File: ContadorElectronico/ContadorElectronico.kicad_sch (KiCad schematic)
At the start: 27 parts, among them J1 Screw_Terminal_01x02, J2 Screw_Terminal_01x02, SW1 MODE, SW2 INC, SW3 DEC, U4 LM358, U5 4N35, U6 4N35

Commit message: First PCB design
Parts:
- removed F?: Fuse, symbol Device:Fuse
- J1: value Screw_Terminal_01x02 -> POWER
- J2: value Screw_Terminal_01x02 -> INPUT
- gave numbers to parts that had none: 1
- renumbered D2 to #D1, D1 to D2, U1 to U2
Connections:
- net +5V: now also J1.1 (Pin_1)
- net GND: now also #U1.2 (IN-), J1.2 (Pin_2)
- net +24V: now reaches #D1.2 (A)
- net +24V: no longer J1.1 (Pin_1)
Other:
- note added: "POWER CONDITIONING"
- moved on the sheet: A1, D2, J1, J2, R1, R10, R11, R12, R2, R3, R4, R5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

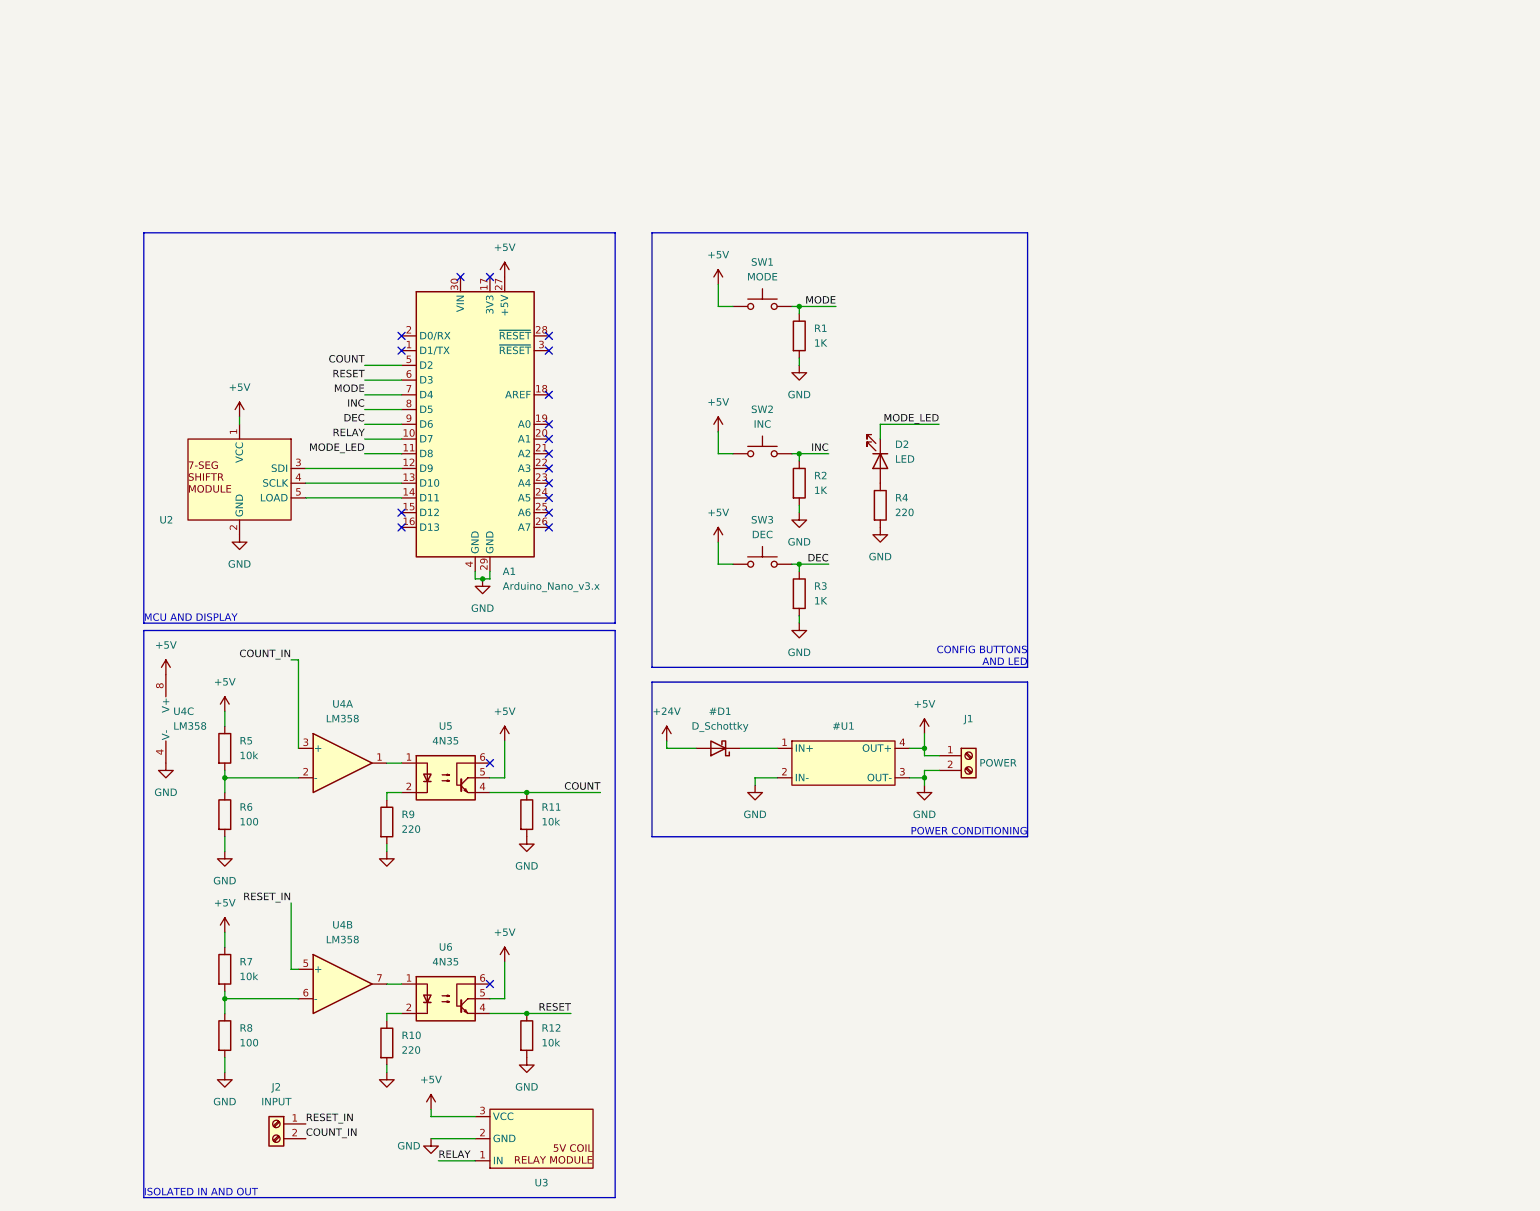
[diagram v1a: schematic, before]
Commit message: PCB done, 5V direct to Arduino
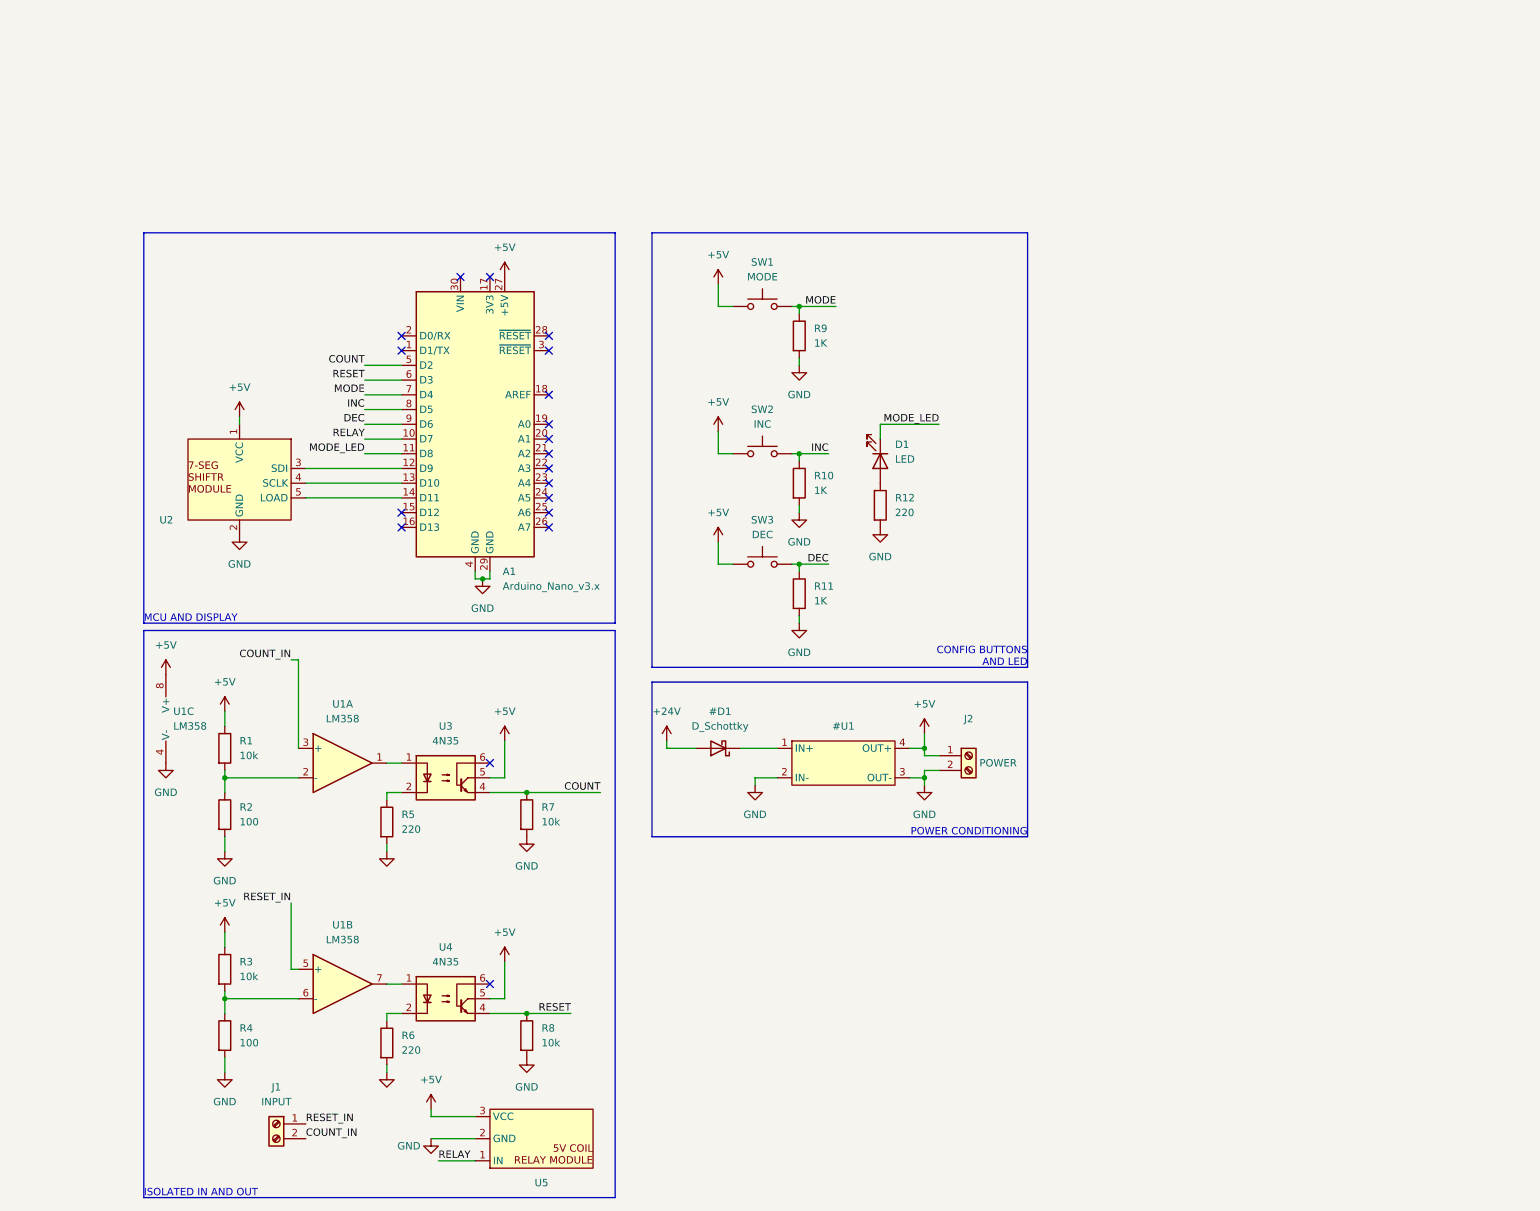
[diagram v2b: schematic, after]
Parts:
- renumbered D2 to D1, J2 to J1, J1 to J2, R5 to R1, R2 to R10, R3 to R11, R4 to R12, R6 to R2, R7 to R3, R8 to R4, R9 to R5, R10 to R6, R11 to R7, R12 to R8, R1 to R9, U4 to U1, U5 to U3, U6 to U4, U3 to U5

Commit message: Diseño inicial
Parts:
- removed #D1: D_Schottky, Diode_THT:D_DO-15_P12.70mm_Horizontal, symbol Device:D_Schottky
- removed J1: INPUT, TerminalBlock:TerminalBlock_bornier-2_P5.08mm, symbol Connector:Screw_Terminal_01x02
- removed J2: POWER, TerminalBlock:TerminalBlock_bornier-2_P5.08mm, symbol Connector:Screw_Terminal_01x02
- added D1: 1N4002, Diode_THT:D_DO-41_SOD81_P10.16mm_Horizontal, symbol Diode:1N4002
- added J1: Screw_Terminal_01x03, TerminalBlock:TerminalBlock_bornier-3_P5.08mm, symbol Connector:Screw_Terminal_01x03
- added J2, J3, J4, J5, J6, J7, J8: Conn_01x01_Pin, Connector:Banana_Jack_1Pin, symbol Connector:Conn_01x01_Pin
- R1, R10, R11, R12, R2, R3, R4, R5, R6, R7, R8, R9: footprint Resistor_THT:R_Axial_DIN0207_L6.3mm_D2.5mm_P10.16mm_Horizontal -> Resistor_SMD:R_0603_1608Metric_Pad0.98x0.95mm_HandSolder
- SW1_MODE1: renamed from SW1; footprint Custom:SW Header -> Button_Switch_THT:SW_PUSH_6mm
- SW2_INC1: renamed from SW2; footprint Custom:SW Header -> Button_Switch_THT:SW_PUSH_6mm
- SW3_DEC1: renamed from SW3; footprint Custom:SW Header -> Button_Switch_THT:SW_PUSH_6mm
- U2: footprint Connector_PinSocket_2.54mm:PinSocket_1x05_P2.54mm_Vertical -> Custom:2Digit7SEG
- U6: renamed from #U1; footprint (none) -> Custom:LM2596 MODULE
- renumbered D1 to D2
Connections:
- net +24V: now also D1.2 (A), J7.1 (Pin_1)
- net +5V: no longer U6.4 (OUT+)
- net COUNT_IN: now also J6.1 (Pin_1)
- net GND: now also J8.1 (Pin_1)
- net RESET_IN: now also J2.1 (Pin_1)
- net at U6.1 (IN+): now also D1.1 (K)
- net +9V: now reaches A1.30 (VIN)
- net +9V: now also U6.4 (OUT+)
- new net COM: J1.2 (Pin_2), J4.1 (Pin_1)
- new net NC: J1.1 (Pin_1), J3.1 (Pin_1)
- new net NO: J1.3 (Pin_3), J5.1 (Pin_1)
- no-connect marks 19 -> 18

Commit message: Working version #1
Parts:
- removed J6: Conn_01x01_Pin, Connector:Banana_Jack_1Pin, symbol Connector:Conn_01x01_Pin
- removed R1, R3: 10k, Resistor_SMD:R_0603_1608Metric_Pad0.98x0.95mm_HandSolder, symbol Device:R
- removed R2, R4: 100, Resistor_SMD:R_0603_1608Metric_Pad0.98x0.95mm_HandSolder, symbol Device:R
- removed U1: LM358, Package_DIP:DIP-8_W7.62mm_Socket, symbol Amplifier_Operational:LM358
- added J1: Conn_01x01_Pin, Connector:Banana_Jack_1Pin, symbol Connector:Conn_01x01_Pin
- R1: renamed from R5; value 220 -> 10k; footprint Resistor_SMD:R_0603_1608Metric_Pad0.98x0.95mm_HandSolder -> Resistor_SMD:R_1206_3216Metric_Pad1.30x1.75mm_HandSolder
- R2: renamed from R6; value 220 -> 10k; footprint Resistor_SMD:R_0603_1608Metric_Pad0.98x0.95mm_HandSolder -> Resistor_SMD:R_1206_3216Metric_Pad1.30x1.75mm_HandSolder
- R3: renamed from R7; footprint Resistor_SMD:R_0603_1608Metric_Pad0.98x0.95mm_HandSolder -> Resistor_SMD:R_1206_3216Metric_Pad1.30x1.75mm_HandSolder
- R4: renamed from R8; footprint Resistor_SMD:R_0603_1608Metric_Pad0.98x0.95mm_HandSolder -> Resistor_SMD:R_1206_3216Metric_Pad1.30x1.75mm_HandSolder
- R5: renamed from R9; footprint Resistor_SMD:R_0603_1608Metric_Pad0.98x0.95mm_HandSolder -> Resistor_SMD:R_1206_3216Metric_Pad1.30x1.75mm_HandSolder
- R6: renamed from R10; footprint Resistor_SMD:R_0603_1608Metric_Pad0.98x0.95mm_HandSolder -> Resistor_SMD:R_1206_3216Metric_Pad1.30x1.75mm_HandSolder
- R7: renamed from R11; footprint Resistor_SMD:R_0603_1608Metric_Pad0.98x0.95mm_HandSolder -> Resistor_SMD:R_1206_3216Metric_Pad1.30x1.75mm_HandSolder
- R8: renamed from R12; footprint Resistor_SMD:R_0603_1608Metric_Pad0.98x0.95mm_HandSolder -> Resistor_SMD:R_1206_3216Metric_Pad1.30x1.75mm_HandSolder
- renumbered J1 to J3, J3 to J4, J4 to J5, J5 to J6, U2 to U1, U3 to U2, U4 to U3, U5 to U4, U6 to U5
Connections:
- net +5V: now also U5.4 (OUT+)
- net COUNT: now also A1.6 (D3); no longer A1.5 (D2)
- net COUNT_IN: now also J2.1 (Pin_1), U2.1
- net DEC: now also A1.8 (D5); no longer A1.9 (D6)
- net INC: now also A1.10 (D7); no longer A1.8 (D5)
- net MODE: now also A1.11 (D8); no longer A1.7 (D4)
- net MODE_LED: now also A1.9 (D6); no longer A1.11 (D8)
- net RELAY: now also A1.7 (D4); no longer A1.10 (D7)
- net RESET: now also A1.5 (D2); no longer A1.6 (D3)
- net RESET_IN: now also U3.1, J1.1 (Pin_1); no longer J2.1 (Pin_1)
- net at A1.12 (D9): now also U1.5 (LOAD); no longer U1.3 (SDI)
- net at A1.14 (D11): now also U1.3 (SDI); no longer U1.5 (LOAD)
- net +24V: no longer names the net of D1.2 (A), J7.1 (Pin_1)
- net +9V: no longer names the net of A1.30 (VIN)
- net +9V: no longer U5.4 (OUT+)
- no-connect marks 18 -> 19
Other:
- moved on the sheet: J3, J4, J5, J6, R1, R2, R3, R4, U2, U3, U4

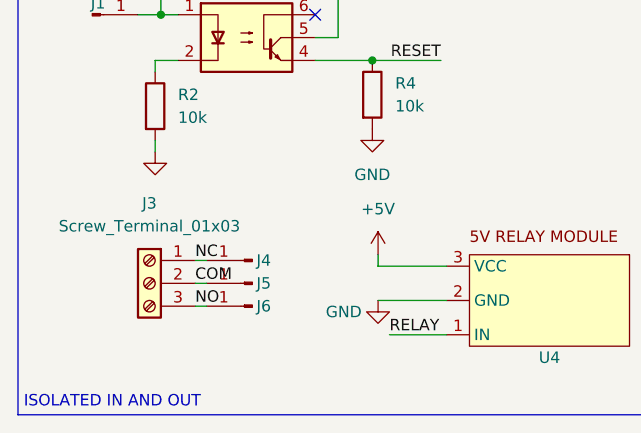
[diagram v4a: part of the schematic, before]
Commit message: ajustes a la PCB
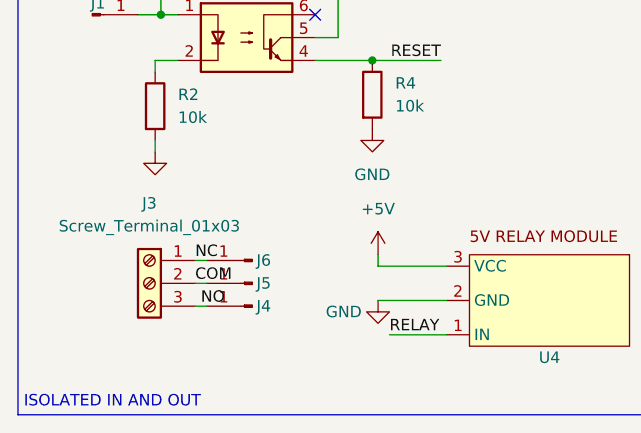
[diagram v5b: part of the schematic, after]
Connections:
- net NC: now also J6.1 (Pin_1); no longer J4.1 (Pin_1)
- net NO: now also J4.1 (Pin_1); no longer J6.1 (Pin_1)
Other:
- moved on the sheet: J4, J6
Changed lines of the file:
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@@
+    (stroke (width 0) (type default))
+  )
+  (wire (pts (xy 53.975 195.58) (xy 55.245 195.58))
     (stroke (width 0) (type default))
   )
@@
     (stroke (width 0) (type default))
   )
-  (wire (pts (xy 53.975 195.58) (xy 55.245 195.58))
-    (stroke (width 0) (type default))
-  )
   (wire (pts (xy 67.31 168.275) (xy 73.66 168.275))
     (stroke (width 0) (type default))
@@
     (stroke (width 0) (type default))
   )
+  (wire (pts (xy 69.85 99.06) (xy 69.85 93.98))
+    (stroke (width 0) (type default))
+  )
+  (wire (pts (xy 161.29 86.36) (xy 161.29 88.9))
+    (stroke (width 0) (type default))
+  )
+  (wire (pts (xy 147.32 111.76) (xy 147.32 110.49))
+    (stroke (width 0) (type default))
+  )
+  (wire (pts (xy 135.89 66.04) (xy 133.35 66.04))
+    (stroke (width 0) (type default))
+  )
+  (wire (pts (xy 168.91 148.59) (xy 168.91 147.32))
+    (stroke (width 0) (type default))
+  )
+  (wire (pts (xy 147.32 119.38) (xy 147.32 120.65))
+    (stroke (width 0) (type default))
+  )
+  (wire (pts (xy 49.53 139.065) (xy 49.53 140.335))
+    (stroke (width 0) (type default))
+  )
+  (wire (pts (xy 50.8 86.36) (xy 50.8 85.09))
+    (stroke (width 0) (type default))
+  )
+  (wire (pts (xy 147.32 92.71) (xy 147.32 91.44))
+    (stroke (width 0) (type default))
+  )
+  (wire (pts (xy 49.53 168.275) (xy 52.07 168.275))
+    (stroke (width 0) (type default))
+  )
+  (wire (pts (xy 81.915 191.135) (xy 74.295 191.135))
+    (stroke (width 0) (type default))
+  )
+  (wire (pts (xy 49.53 147.955) (xy 49.53 149.225))
+    (stroke (width 0) (type default))
+  )
+  (wire (pts (xy 73.66 139.065) (xy 86.36 139.065))
+    (stroke (width 0) (type default))
+  )
+  (wire (pts (xy 171.45 86.36) (xy 161.29 86.36))
+    (stroke (width 0) (type default))
+  )
+  (wire (pts (xy 50.165 163.195) (xy 52.07 163.195))
+    (stroke (width 0) (type default))
+  )
+  (wire (pts (xy 72.39 86.36) (xy 78.74 86.36))
+    (stroke (width 0) (type default))
+  )
+  (wire (pts (xy 147.32 91.44) (xy 152.4 91.44))
+    (stroke (width 0) (type default))
+  )
+  (wire (pts (xy 72.39 91.44) (xy 78.74 91.44))
+    (stroke (width 0) (type default))
+  )
+  (wire (pts (xy 74.295 191.135) (xy 74.295 189.865))
+    (stroke (width 0) (type default))
+  )
   (wire (pts (xy 53.975 190.5) (xy 55.245 190.5))
-    (stroke (width 0) (type default))
-  )
-  (wire (pts (xy 69.85 99.06) (xy 69.85 93.98))
-    (stroke (width 0) (type default))
-  )
-  (wire (pts (xy 161.29 86.36) (xy 161.29 88.9))
-    (stroke (width 0) (type default))
-  )
-  (wire (pts (xy 147.32 111.76) (xy 147.32 110.49))
-    (stroke (width 0) (type default))
-  )
-  (wire (pts (xy 135.89 66.04) (xy 133.35 66.04))
-    (stroke (width 0) (type default))
-  )
-  (wire (pts (xy 168.91 148.59) (xy 168.91 147.32))
-    (stroke (width 0) (type default))
-  )
-  (wire (pts (xy 147.32 119.38) (xy 147.32 120.65))
-    (stroke (width 0) (type default))
-  )
-  (wire (pts (xy 49.53 139.065) (xy 49.53 140.335))
-    (stroke (width 0) (type default))
-  )
-  (wire (pts (xy 50.8 86.36) (xy 50.8 85.09))
-    (stroke (width 0) (type default))
-  )
-  (wire (pts (xy 147.32 92.71) (xy 147.32 91.44))
-    (stroke (width 0) (type default))
-  )
-  (wire (pts (xy 49.53 168.275) (xy 52.07 168.275))
-    (stroke (width 0) (type default))
-  )
-  (wire (pts (xy 81.915 191.135) (xy 74.295 191.135))
-    (stroke (width 0) (type default))
-  )
-  (wire (pts (xy 49.53 147.955) (xy 49.53 149.225))
-    (stroke (width 0) (type default))
-  )
-  (wire (pts (xy 73.66 139.065) (xy 86.36 139.065))
-    (stroke (width 0) (type default))
-  )
-  (wire (pts (xy 171.45 86.36) (xy 161.29 86.36))
-    (stroke (width 0) (type default))
-  )
-  (wire (pts (xy 50.165 163.195) (xy 52.07 163.195))
-    (stroke (width 0) (type default))
-  )
-  (wire (pts (xy 72.39 86.36) (xy 78.74 86.36))
-    (stroke (width 0) (type default))
-  )
-  (wire (pts (xy 147.32 91.44) (xy 152.4 91.44))
-    (stroke (width 0) (type default))
-  )
-  (wire (pts (xy 72.39 91.44) (xy 78.74 91.44))
-    (stroke (width 0) (type default))
-  )
-  (wire (pts (xy 74.295 191.135) (xy 74.295 189.865))
     (stroke (width 0) (type default))
   )
@@
     (effects (font (size 1.27 1.27)) (justify right bottom))
   )
-  (label "NO" (at 53.975 195.58 0) (fields_autoplaced)
+  (label "NO" (at 54.61 195.58 0) (fields_autoplaced)
     (effects (font (size 1.27 1.27)) (justify left bottom))
   )
@@
     )
   )
-  (symbol (lib_id "Connector:Conn_01x01_Pin") (at 60.325 195.58 0) (mirror y) (unit 1)
+  (symbol (lib_id "Connector:Conn_01x01_Pin") (at 60.325 190.5 0) (mirror y) (unit 1)
     (in_bom yes) (on_board yes) (dnp no)
-    (property "Reference" "J6" (at 61.595 195.58 0)
-      (effects (font (size 1.27 1.27)))
-    )
-    (property "Value" "Conn_01x01_Pin" (at 59.69 193.04 0)
-      (effects (font (size 1.27 1.27)) hide)
-    )
-    (property "Footprint" "Connector:Banana_Jack_1Pin" (at 60.325 195.58 0)
-      (effects (font (size 1.27 1.27)) hide)
-    )
-    (property "Datasheet" "~" (at 60.325 195.58 0)
+    (property "Reference" "J6" (at 61.595 190.5 0)
+      (effects (font (size 1.27 1.27)))
+    )
+    (property "Value" "Conn_01x01_Pin" (at 59.69 187.96 0)
+      (effects (font (size 1.27 1.27)) hide)
+    )
+    (property "Footprint" "Connector:Banana_Jack_1Pin" (at 60.325 190.5 0)
+      (effects (font (size 1.27 1.27)) hide)
+    )
+    (property "Datasheet" "~" (at 60.325 190.5 0)
       (effects (font (size 1.27 1.27)) hide)
     )
@@
     )
   )
-  (symbol (lib_id "Connector:Conn_01x01_Pin") (at 60.325 190.5 0) (mirror y) (unit 1)
+  (symbol (lib_id "Connector:Conn_01x01_Pin") (at 60.325 195.58 0) (mirror y) (unit 1)
     (in_bom yes) (on_board yes) (dnp no)
-    (property "Reference" "J4" (at 61.595 190.5 0)
-      (effects (font (size 1.27 1.27)))
-    )
-    (property "Value" "Conn_01x01_Pin" (at 59.69 187.96 0)
-      (effects (font (size 1.27 1.27)) hide)
-    )
-    (property "Footprint" "Connector:Banana_Jack_1Pin" (at 60.325 190.5 0)
-      (effects (font (size 1.27 1.27)) hide)
-    )
-    (property "Datasheet" "~" (at 60.325 190.5 0)
-      (effects (font (size 1.27 1.27)) hide)
-    )
+    (property "Reference" "J4" (at 61.595 195.58 0)
+      (effects (font (size 1.27 1.27)))
+    )
+    (property "Value" "Conn_01x01_Pin" (at 59.69 193.04 0)
+      (effects (font (size 1.27 1.27)) hide)
+    )
+    (property "Footprint" "Connector:Banana_Jack_1Pin" (at 60.325 195.58 0)
+      (effects (font (size 1.27 1.27)) hide)
+    )
+    (property "Datasheet" "~" (at 60.325 195.58 0)
+      (effects (font (size 1.27 1.27)) hide)
+    )
